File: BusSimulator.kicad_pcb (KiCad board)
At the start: 2 copper layers, 101.6 x 53.3 mm, 17 parts, among them J1 CONN_3-6318491-6, J2 CONN_3-6318491-6, U1 MPM3620, U2 MPM3620

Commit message: logo
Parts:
- added G1: LOGO, BusSimulator:LetSatLogo440, F.Cu at (195.9, 138.8)
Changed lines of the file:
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@@
     (links 92)
     (no_connects 59)
-    (area 109.924999 88.174999 211.675001 141.675001)
+    (area 108.853572 86.26384 211.882401 142.04484)
     (thickness 1.6)
     (drawings 10)
     (tracks 170)
     (zones 0)
-    (modules 17)
+    (modules 18)
     (nets 204)
   )
@@
       (net 16 GNDREF))
   )
+  (module BusSimulator:LetSatLogo440 (layer F.Cu)
+    (at 195.925 138.775)
+    (fp_text reference G1 (at 0 0) (layer F.SilkS) hide
+      (effects (font (thickness 0.3)))
+    )
+    (fp_text value LOGO (at 0.75 0) (layer F.SilkS) hide
+      (effects (font (thickness 0.3)))
+    )
+    (fp_poly (pts (xy 14.374091 -1.27) (xy 12.524543 -1.27) (xy 11.86217 -1.267926) (xy 11.301042 -1.260868)
+      (xy 10.827009 -1.247571) (xy 10.425923 -1.226781) (xy 10.083634 -1.197245) (xy 9.785993 -1.157707)
+      (xy 9.51885 -1.106914) (xy 9.268056 -1.043611) (xy 9.019462 -0.966544) (xy 8.990302 -0.956718)
+      (xy 8.295805 -0.66214) (xy 7.651998 -0.271547) (xy 7.070416 0.204436) (xy 6.562591 0.755186)
+      (xy 6.140059 1.370077) (xy 5.86025 1.926575) (xy 5.697679 2.309091) (xy 4.690238 2.309091)
+      (xy 4.830611 1.922368) (xy 5.178079 1.127685) (xy 5.615969 0.40227) (xy 6.138743 -0.248783)
+      (xy 6.740859 -0.820381) (xy 7.416777 -1.307428) (xy 8.160957 -1.704832) (xy 8.967859 -2.007498)
+      (xy 9.166755 -2.064535) (xy 9.308939 -2.102348) (xy 9.437794 -2.133407) (xy 9.566419 -2.158498)
+      (xy 9.70791 -2.178408) (xy 9.875366 -2.193924) (xy 10.081885 -2.205834) (xy 10.340563 -2.214924)
+      (xy 10.6645 -2.221982) (xy 11.066791 -2.227793) (xy 11.560536 -2.233146) (xy 12.050568 -2.237818)
+      (xy 14.374091 -2.25951) (xy 14.374091 -1.27)) (layer F.Cu) (width 0.01))
+    (fp_poly (pts (xy 12.353636 2.309091) (xy 11.314545 2.309091) (xy 11.314545 -0.750455) (xy 12.353636 -0.750455)
+      (xy 12.353636 2.309091)) (layer F.Cu) (width 0.01))
+    (fp_poly (pts (xy 14.374091 -1.27) (xy 12.524543 -1.27) (xy 11.86217 -1.267926) (xy 11.301042 -1.260868)
+      (xy 10.827009 -1.247571) (xy 10.425923 -1.226781) (xy 10.083634 -1.197245) (xy 9.785993 -1.157707)
+      (xy 9.51885 -1.106914) (xy 9.268056 -1.043611) (xy 9.019462 -0.966544) (xy 8.990302 -0.956718)
+      (xy 8.295805 -0.66214) (xy 7.651998 -0.271547) (xy 7.070416 0.204436) (xy 6.562591 0.755186)
+      (xy 6.140059 1.370077) (xy 5.86025 1.926575) (xy 5.697679 2.309091) (xy 4.690238 2.309091)
+      (xy 4.830611 1.922368) (xy 5.178079 1.127685) (xy 5.615969 0.40227) (xy 6.138743 -0.248783)
+      (xy 6.740859 -0.820381) (xy 7.416777 -1.307428) (xy 8.160957 -1.704832) (xy 8.967859 -2.007498)
+      (xy 9.166755 -2.064535) (xy 9.308939 -2.102348) (xy 9.437794 -2.133407) (xy 9.566419 -2.158498)
+      (xy 9.70791 -2.178408) (xy 9.875366 -2.193924) (xy 10.081885 -2.205834) (xy 10.340563 -2.214924)
+      (xy 10.6645 -2.221982) (xy 11.066791 -2.227793) (xy 11.560536 -2.233146) (xy 12.050568 -2.237818)
+      (xy 14.374091 -2.25951) (xy 14.374091 -1.27)) (layer F.Mask) (width 0.01))
+    (fp_poly (pts (xy 12.353636 2.309091) (xy 11.314545 2.309091) (xy 11.314545 -0.750455) (xy 12.353636 -0.750455)
+      (xy 12.353636 2.309091)) (layer F.Mask) (width 0.01))
+    (fp_poly (pts (xy -13.667671 -0.736023) (xy -13.6525 1.298863) (xy -10.621777 1.298863) (xy -10.621819 2.309091)
+      (xy -14.662728 2.309091) (xy -14.662728 -2.770909) (xy -13.682841 -2.770909) (xy -13.667671 -0.736023)) (layer F.SilkS) (width 0.01))
+    (fp_poly (pts (xy -6.523182 0.288636) (xy -8.605859 0.288636) (xy -8.58918 0.79375) (xy -8.5725 1.298863)
+      (xy -7.042728 1.310372) (xy -5.512955 1.321881) (xy -5.496276 1.815486) (xy -5.479596 2.309091)
+      (xy -9.582728 2.309091) (xy -9.582728 -0.750455) (xy -6.523182 -0.750455) (xy -6.523182 0.288636)) (layer F.SilkS) (width 0.01))
+    (fp_poly (pts (xy -2.958523 -0.738271) (xy -2.453409 -0.721591) (xy -2.422629 2.309091) (xy -3.463637 2.309091)
+      (xy -3.463637 -0.75495) (xy -2.958523 -0.738271)) (layer F.SilkS) (width 0.01))
+    (fp_poly (pts (xy 1.497471 -0.74795) (xy 1.896073 -0.738379) (xy 2.21182 -0.718657) (xy 2.460978 -0.685701)
+      (xy 2.659811 -0.636426) (xy 2.824587 -0.567749) (xy 2.971569 -0.476584) (xy 3.117024 -0.359847)
+      (xy 3.13287 -0.345981) (xy 3.404018 -0.03861) (xy 3.57669 0.306077) (xy 3.654188 0.670892)
+      (xy 3.639817 1.038648) (xy 3.536881 1.392158) (xy 3.348682 1.714235) (xy 3.078525 1.987693)
+      (xy 2.729714 2.195344) (xy 2.637216 2.23254) (xy 2.50326 2.258125) (xy 2.256329 2.278267)
+      (xy 1.898779 2.292861) (xy 1.432966 2.3018) (xy 1.024659 2.304699) (xy -0.404091 2.309091)
+      (xy -0.404091 1.327727) (xy 0.867763 1.327727) (xy 1.349503 1.3253) (xy 1.729122 1.316392)
+      (xy 2.019884 1.298563) (xy 2.235053 1.26937) (xy 2.387891 1.226373) (xy 2.491662 1.16713)
+      (xy 2.559629 1.089201) (xy 2.598094 1.009261) (xy 2.650531 0.793553) (xy 2.612723 0.619426)
+      (xy 2.486713 0.457377) (xy 2.411758 0.386036) (xy 2.340291 0.338311) (xy 2.248207 0.309456)
+      (xy 2.111407 0.294723) (xy 1.905788 0.289366) (xy 1.629978 0.288636) (xy 1.158536 0.274068)
+      (xy 0.780369 0.225645) (xy 0.476448 0.136287) (xy 0.22774 -0.001086) (xy 0.015217 -0.193555)
+      (xy -0.120588 -0.362611) (xy -0.207648 -0.483916) (xy -0.26347 -0.576875) (xy -0.277165 -0.645255)
+      (xy -0.237846 -0.692828) (xy -0.134623 -0.723362) (xy 0.04339 -0.740626) (xy 0.307082 -0.74839)
+      (xy 0.667341 -0.750424) (xy 0.999749 -0.750455) (xy 1.497471 -0.74795)) (layer F.SilkS) (width 0.01))
+    (fp_poly (pts (xy 9.318607 0.910594) (xy 9.440983 1.27947) (xy 9.550148 1.611853) (xy 9.641061 1.892114)
+      (xy 9.708679 2.104624) (xy 9.747957 2.233755) (xy 9.755909 2.265821) (xy 9.703776 2.292592)
+      (xy 9.568413 2.30782) (xy 9.38137 2.312407) (xy 9.174199 2.307253) (xy 8.978452 2.293259)
+      (xy 8.825679 2.271325) (xy 8.747431 2.242352) (xy 8.743862 2.236931) (xy 8.717748 2.16153)
+      (xy 8.661322 1.995026) (xy 8.580788 1.755845) (xy 8.482351 1.462414) (xy 8.372213 1.133157)
+      (xy 8.369716 1.125681) (xy 8.24534 0.756685) (xy 8.155402 0.481075) (xy 8.102272 0.281322)
+      (xy 8.088322 0.1399) (xy 8.115925 0.039281) (xy 8.18745 -0.038061) (xy 8.30527 -0.109654)
+      (xy 8.471757 -0.193025) (xy 8.553721 -0.234215) (xy 8.881305 -0.401364) (xy 9.318607 0.910594)) (layer F.SilkS) (width 0.01))
+    (fp_poly (pts (xy 7.631314 -2.019188) (xy 7.363462 -1.874776) (xy 7.082892 -1.707016) (xy 6.844508 -1.548963)
+      (xy 6.816286 -1.528507) (xy 6.46513 -1.27) (xy -9.582728 -1.27) (xy -9.582728 -2.251364)
+      (xy 8.095187 -2.251364) (xy 7.631314 -2.019188)) (layer F.SilkS) (width 0.01))
+  )
   (gr_line (start 110 88.25) (end 207.525 88.25) (layer Edge.Cuts) (width 0.15))

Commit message: fixed connector for mcom
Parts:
- moved J1 6.56 mm to (127.2, 94.5)
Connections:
- J1 pad 1: GND -> (no net)
- J1 pad 10: GBE0_MDI1+ -> (no net)
- J1 pad 100: GND -> (no net)
- J1 pad 101: Net-(J1-Pad101) -> (no net)
- J1 pad 102: Net-(J1-Pad102) -> (no net)
- J1 pad 103: LIDn -> (no net)
- J1 pad 104: VCC_12V -> (no net)
- J1 pad 105: VCC_12V -> (no net)
- J1 pad 106: VCC_12V -> (no net)
- J1 pad 107: VCC_12V -> (no net)
- J1 pad 108: VCC_12V -> (no net)
- J1 pad 109: VCC_12V -> (no net)
- J1 pad 11: GND -> (no net)
- J1 pad 110: GND -> (no net)
- J1 pad 111: GND -> (no net)
- J1 pad 112: GBE0_ACTn -> (no net)
- J1 pad 113: Net-(J1-Pad113) -> (no net)
- J1 pad 114: Net-(J1-Pad114) -> (no net)
- J1 pad 115: Net-(J1-Pad115) -> (no net)
- J1 pad 116: Net-(J1-Pad116) -> (no net)
- J1 pad 117: Net-(J1-Pad117) -> (no net)
- J1 pad 118: Net-(J1-Pad118) -> (no net)
- J1 pad 119: Net-(J1-Pad119) -> (no net)
- J1 pad 12: GBE0_MDI0- -> (no net)
- J1 pad 120: Net-(J1-Pad120) -> (no net)
- J1 pad 121: GND -> (no net)
- J1 pad 122: PWRBTNn -> (no net)
- J1 pad 123: Net-(J1-Pad123) -> (no net)
- J1 pad 124: Net-(J1-Pad124) -> (no net)
- J1 pad 125: Net-(J1-Pad125) -> (no net)
- J1 pad 126: Net-(J1-Pad126) -> (no net)
- J1 pad 127: Net-(J1-Pad127) -> (no net)
- J1 pad 128: Net-(J1-Pad128) -> (no net)
- J1 pad 129: Net-(J1-Pad129) -> (no net)
- J1 pad 13: GBE0_MDI0+ -> (no net)
- J1 pad 130: Net-(J1-Pad130) -> (no net)
- J1 pad 131: GND -> (no net)
- J1 pad 132: USB_SSTX0- -> (no net)
- J1 pad 133: USB_SSTX0+ -> (no net)
- J1 pad 134: PWR_OK -> (no net)
- J1 pad 135: Net-(J1-Pad135) -> (no net)
- J1 pad 136: Net-(J1-Pad136) -> (no net)
- J1 pad 137: Net-(J1-Pad137) -> (no net)
- J1 pad 138: Net-(J1-Pad138) -> (no net)
- J1 pad 139: Net-(J1-Pad139) -> (no net)
- J1 pad 14: GBE0_CTREF(GND) -> (no net)
- J1 pad 140: AC/HDA_SDIN0 -> (no net)
- J1 pad 141: GND -> (no net)
- J1 pad 142: Net-(J1-Pad142) -> (no net)
- J1 pad 143: I2C_CK -> (no net)
- J1 pad 144: I2C_DAT -> (no net)
- J1 pad 145: THRMn -> (no net)
- J1 pad 146: Net-(J1-Pad146) -> (no net)
- J1 pad 147: Net-(J1-Pad147) -> (no net)
- J1 pad 148: USB_4_5_OCn -> (no net)
- J1 pad 149: USB5- -> (no net)
- J1 pad 15: Net-(J1-Pad15) -> (no net)
- J1 pad 150: USB5+ -> (no net)
- J1 pad 151: GND -> (no net)
- J1 pad 152: USB3- -> (no net)
- J1 pad 153: USB3+ -> (no net)
- J1 pad 154: USB_0_1_OCn -> (no net)
- J1 pad 155: USB1- -> (no net)
- J1 pad 156: USB1+ -> (no net)
- J1 pad 157: Net-(J1-Pad157) -> (no net)
- J1 pad 158: EXCD1_CPPEn -> (no net)
- J1 pad 159: SYS_RESETn -> (no net)
- J1 pad 16: SATA0_TX+ -> (no net)
- J1 pad 160: CB_RESETn -> (no net)
- J1 pad 161: GND -> (no net)
- J1 pad 162: Net-(J1-Pad162) -> (no net)
- J1 pad 163: Net-(J1-Pad163) -> (no net)
- J1 pad 164: GPO1 -> (no net)
- J1 pad 165: Net-(J1-Pad165) -> (no net)
- J1 pad 166: Net-(J1-Pad166) -> (no net)
- J1 pad 167: GPO2 -> (no net)
- J1 pad 168: Net-(J1-Pad168) -> (no net)
- J1 pad 169: Net-(J1-Pad169) -> (no net)
- J1 pad 17: SATA0_TX- -> (no net)
- J1 pad 170: GND -> (no net)
- J1 pad 171: Net-(J1-Pad171) -> (no net)
- J1 pad 172: Net-(J1-Pad172) -> (no net)
- J1 pad 173: GPO3 -> (no net)
- J1 pad 174: PCIE_RX1+ -> (no net)
- J1 pad 175: PCIE_RX1- -> (no net)
- J1 pad 176: WAKE0n -> (no net)
- J1 pad 177: WAKE1n -> (no net)
- J1 pad 178: PCIE_RX0+ -> (no net)
- J1 pad 179: PCIE_RX0- -> (no net)
- J1 pad 18: Net-(J1-Pad18) -> (no net)
- J1 pad 180: GND -> (no net)
- J1 pad 181: DDIO_PAIR0+ -> (no net)
- J1 pad 182: DDIO_PAIR0- -> (no net)
- J1 pad 183: DDIO_PAIR1+ -> (no net)
- J1 pad 184: DDIO_PAIR1- -> (no net)
- J1 pad 185: DDIO_PAIR2+ -> (no net)
- J1 pad 186: DDIO_PAIR2- -> (no net)
- J1 pad 187: Net-(J1-Pad187) -> (no net)
- J1 pad 188: Net-(J1-Pad188) -> (no net)
- J1 pad 189: LVDS_BKLT_EN -> (no net)
- J1 pad 19: SATA0_RX+ -> (no net)
- J1 pad 190: GND -> (no net)
- J1 pad 191: DDIO_PAIR3+ -> (no net)
- J1 pad 192: DDIO_PAIR3- -> (no net)
- J1 pad 193: LVDS_BKLT_CTRL -> (no net)
- J1 pad 194: VCC_5V_SBY -> (no net)
- J1 pad 195: VCC_5V_SBY -> (no net)
- J1 pad 196: VCC_5V_SBY -> (no net)
- J1 pad 197: VCC_5V_SBY -> (no net)
- J1 pad 198: Net-(J1-Pad198) -> (no net)
- J1 pad 199: DDIO_HPD -> (no net)
- J1 pad 2: GBE0_MDI3- -> (no net)
- J1 pad 20: SATA0_RX- -> (no net)
- J1 pad 200: GND -> (no net)
- J1 pad 201: Net-(J1-Pad201) -> (no net)
- J1 pad 202: Net-(J1-Pad202) -> (no net)
- J1 pad 203: Net-(J1-Pad203) -> (no net)
- J1 pad 204: Net-(J1-Pad204) -> (no net)
- J1 pad 205: DDIO_DDC_AUX_SEL -> (no net)
- J1 pad 206: Net-(J1-Pad206) -> (no net)
- J1 pad 207: SPI_CSn -> (no net)
- J1 pad 208: DDIO_CTRLCLK_AUX+ -> (no net)
- J1 pad 209: DDIO_CTRLDATA_AUX- -> (no net)
- J1 pad 21: GND -> (no net)
- J1 pad 210: GND -> (no net)
- J1 pad 211: FAN_PWMOUTn -> (no net)
- J1 pad 212: FAN_TACHINn -> (no net)
- J1 pad 213: SLEEPn -> (no net)
- J1 pad 214: VCC_12V -> (no net)
- J1 pad 215: VCC_12V -> (no net)
- J1 pad 216: VCC_12V -> (no net)
- J1 pad 217: VCC_12V -> (no net)
- J1 pad 218: VCC_12V -> (no net)
- J1 pad 219: VCC_12V -> (no net)
- J1 pad 22: USB_SSRX0- -> (no net)
- J1 pad 220: GND -> (no net)
- J1 pad 23: USB_SSRX0+ -> (no net)
- J1 pad 24: Net-(J1-Pad24) -> (no net)
- J1 pad 25: Net-(J1-Pad25) -> (no net)
- J1 pad 26: Net-(J1-Pad26) -> (no net)
- J1 pad 27: BATLOWn -> (no net)
- J1 pad 28: SATA_ACTn -> (no net)
- J1 pad 29: AC/HDA_SYNC -> (no net)
- J1 pad 3: GBE0_MDI3+ -> (no net)
- J1 pad 30: Net-(J1-Pad30) -> (no net)
- J1 pad 31: GND -> (no net)
- J1 pad 32: AC/HDA_BITCLK -> (no net)
- J1 pad 33: AC/HDA_SDOUT -> (no net)
- J1 pad 34: Net-(J1-Pad34) -> (no net)
- J1 pad 35: Net-(J1-Pad35) -> (no net)
- J1 pad 36: Net-(J1-Pad36) -> (no net)
- J1 pad 37: Net-(J1-Pad37) -> (no net)
- J1 pad 38: Net-(J1-Pad38) -> (no net)
- J1 pad 39: USB4- -> (no net)
- J1 pad 4: GBE0_LINK100n -> (no net)
- J1 pad 40: USB4+ -> (no net)
- J1 pad 41: GND -> (no net)
- J1 pad 42: USB2- -> (no net)
- J1 pad 43: USB2+ -> (no net)
- J1 pad 44: USB_2_3_OCn -> (no net)
- J1 pad 45: USB0- -> (no net)
- J1 pad 46: USB0+ -> (no net)
- J1 pad 47: VCC_RTC -> (no net)
- J1 pad 48: Net-(J1-Pad48) -> (no net)
- J1 pad 49: EXCD0_CPPEn -> (no net)
- J1 pad 5: GBE0_LINK1000n -> (no net)
- J1 pad 50: Net-(J1-Pad50) -> (no net)
- J1 pad 51: GND -> (no net)
- J1 pad 52: Net-(J1-Pad52) -> (no net)
- J1 pad 53: Net-(J1-Pad53) -> (no net)
- J1 pad 54: GPI0 -> (no net)
- J1 pad 55: Net-(J1-Pad55) -> (no net)
- J1 pad 56: Net-(J1-Pad56) -> (no net)
- J1 pad 57: GND -> (no net)
- J1 pad 58: Net-(J1-Pad58) -> (no net)
- J1 pad 59: Net-(J1-Pad59) -> (no net)
- J1 pad 6: GBE0_MDI2- -> (no net)
- J1 pad 60: GND -> (no net)
- J1 pad 61: Net-(J1-Pad61) -> (no net)
- J1 pad 62: Net-(J1-Pad62) -> (no net)
- J1 pad 63: GPI1 -> (no net)
- J1 pad 64: PCIE_TX1+ -> (no net)
- J1 pad 65: PCIE_TX1- -> (no net)
- J1 pad 66: GND -> (no net)
- J1 pad 67: GPI2 -> (no net)
- J1 pad 68: PCIE_TX0+ -> (no net)
- J1 pad 69: PCIE_TX0- -> (no net)
- J1 pad 7: GBE0_MDI2+ -> (no net)
- J1 pad 70: GND -> (no net)
- J1 pad 71: LVDS_A0+ -> (no net)
- J1 pad 72: LVDS_A0- -> (no net)
- J1 pad 73: LVDS_A1+ -> (no net)
- J1 pad 74: LVDS_A1- -> (no net)
- J1 pad 75: LVDS_A2+ -> (no net)
- J1 pad 76: LVDS_A2- -> (no net)
- J1 pad 77: LVD_VDD_EN -> (no net)
- J1 pad 78: LVDS_A3+ -> (no net)
- J1 pad 79: LVDS_A3- -> (no net)
- J1 pad 8: Net-(J1-Pad8) -> (no net)
- J1 pad 80: GND -> (no net)
- J1 pad 81: LVDS_A_CK+ -> (no net)
- J1 pad 82: LVDS_A_CK- -> (no net)
- J1 pad 83: LVDS_I2C_CK -> (no net)
- J1 pad 84: LDVS_I2C_DAT -> (no net)
- J1 pad 85: GPI3 -> (no net)
- J1 pad 86: Net-(J1-Pad86) -> (no net)
- J1 pad 87: eDP_HPD -> (no net)
- J1 pad 88: PCIE_CLK_REF+ -> (no net)
- J1 pad 89: PCIE_CLK_REF- -> (no net)
- J1 pad 9: GBE0_MDI1- -> (no net)
- J1 pad 90: GND -> (no net)
- J1 pad 91: SPI_POWER -> (no net)
- J1 pad 92: SPI_MISO -> (no net)
- J1 pad 93: GPO0 -> (no net)
- J1 pad 94: SPI_CLK -> (no net)
- J1 pad 95: SPI_MOSI -> (no net)
- J1 pad 96: Net-(J1-Pad96) -> (no net)
- J1 pad 97: TYPE10n(GND) -> (no net)
- J1 pad 98: SER0_TX -> (no net)
- J1 pad 99: SER0_RX -> (no net)

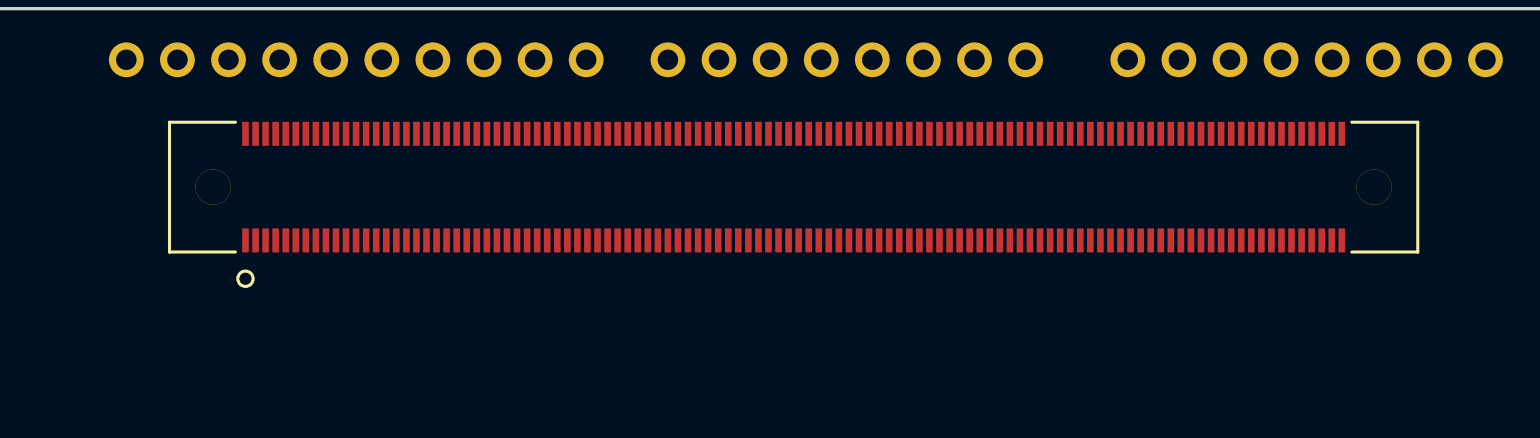
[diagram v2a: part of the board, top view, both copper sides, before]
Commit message: pullled pins to isolate
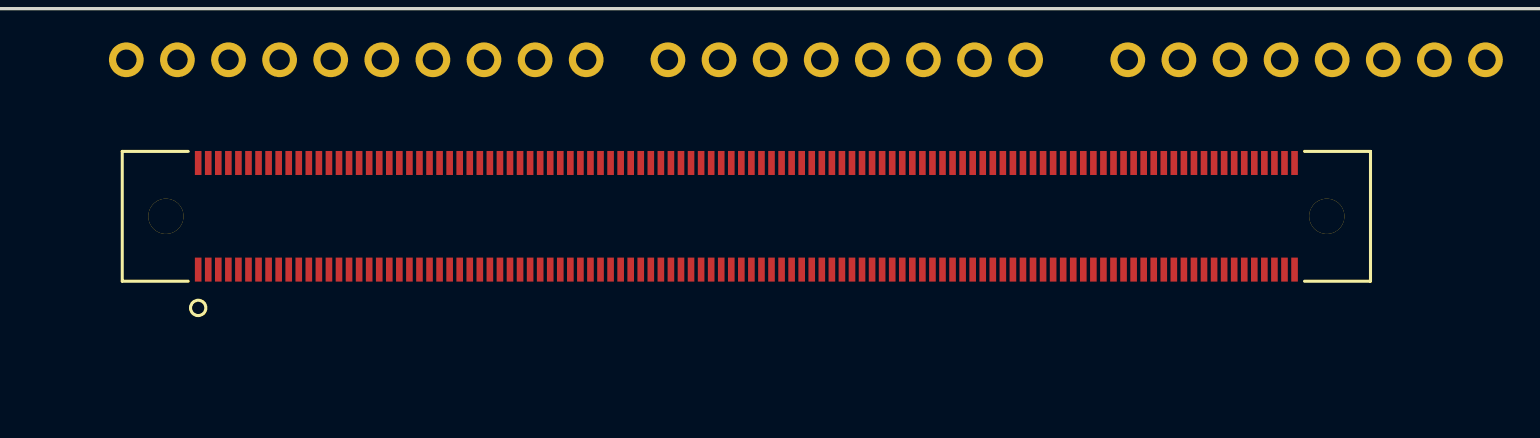
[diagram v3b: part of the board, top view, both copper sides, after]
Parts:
- moved J1 2.76 mm to (124.9, 95.9)
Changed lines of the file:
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@@
     (links 0)
     (no_connects 20)
-    (area 108.853572 86.26384 211.882401 142.04484)
+    (area 109.924999 88.174999 211.675001 141.675001)
     (thickness 1.6)
     (drawings 10)
@@
   )
   (module BusSimulator:ComExpressMini10 (layer F.Cu)
-    (at 127.25 94.475)
+    (at 124.9 95.925)
     (fp_text reference J1 (at 34.725998 2.65) (layer F.SilkS) hide
       (effects (font (size 1 1) (thickness 0.15)))
